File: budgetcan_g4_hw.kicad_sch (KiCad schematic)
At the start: 95 parts, among them IC1 M74VHC1GT66DTT1G, IC2 M74VHC1GT66DTT1G, IC3 M74VHC1GT66DTT1G, J1 USB_C_Receptacle_USB2.0, J3 20021511-00014T4LF, J4 Conn_01x02, J5 348260124, U1 AP22804AW5, U12 TJA1021T, U14 TPS2116DRLR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

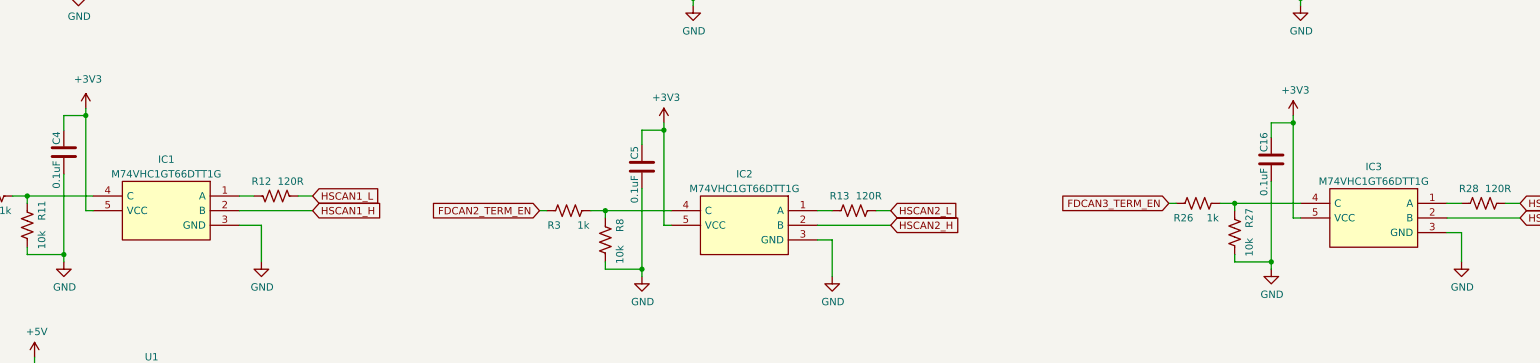
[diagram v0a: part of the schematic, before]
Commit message: Fix the LCSC part number for the CAN termination switch
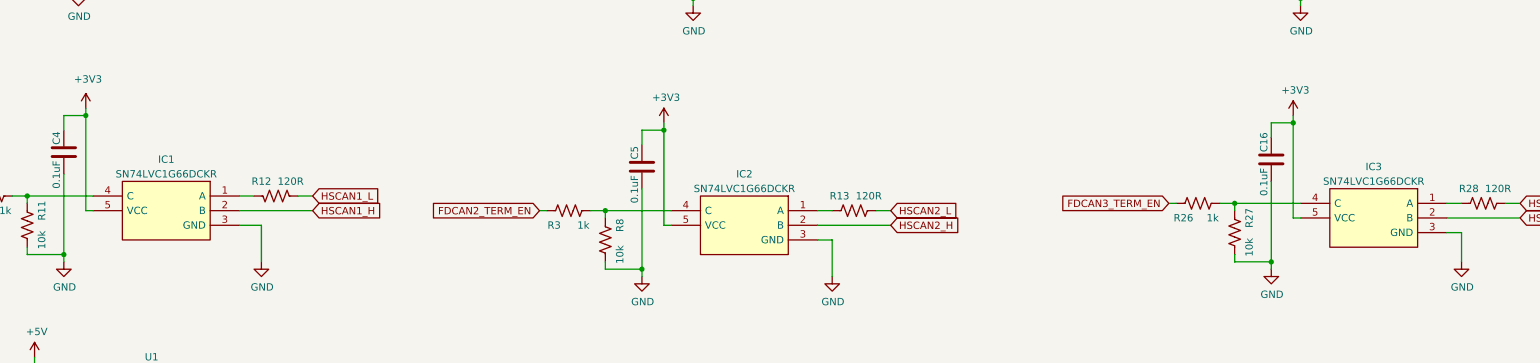
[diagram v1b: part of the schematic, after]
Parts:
- IC1, IC2, IC3: value M74VHC1GT66DTT1G -> SN74LVC1G66DCKR; LCSC Part # C5375974 -> C113518; Mouser Part Number 595-LVC1G66QDCKRQ1 -> (none); Mouser Price/Stock https://www.mouser.co.uk/ProductDetail/Texas-Instruments/SN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 -> (none)
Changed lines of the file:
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@@
       (effects (font (size 1.27 1.27)))
     )
-    (property "Value" "M74VHC1GT66DTT1G" (at 307.34 137.16 0)
+    (property "Value" "SN74LVC1G66DCKR" (at 307.34 137.16 0)
       (effects (font (size 1.27 1.27)))
     )
@@
       (effects (font (size 1.27 1.27)) (justify left) hide)
     )
-    (property "Mouser Part Number" "595-LVC1G66QDCKRQ1" (at 341.63 148.59 0)
-      (effects (font (size 1.27 1.27)) (justify left) hide)
-    )
-    (property "Mouser Price/Stock" "https://www.mouser.co.uk/ProductDetail/Texas-Instruments/SN74LVC1G66QDCKRQ1?qs=pajgIaoyDUhMU131%252BNzplA%3D%3D" (at 341.63 151.13 0)
+    (property "Mouser Part Number" "" (at 341.63 148.59 0)
+      (effects (font (size 1.27 1.27)) (justify left) hide)
+    )
+    (property "Mouser Price/Stock" "" (at 341.63 151.13 0)
       (effects (font (size 1.27 1.27)) (justify left) hide)
     )
@@
       (effects (font (size 1.27 1.27)) (justify left) hide)
     )
-    (property "LCSC Part #" "C5375974" (at 320.04 140.97 0)
+    (property "LCSC Part #" "C113518" (at 320.04 140.97 0)
       (effects (font (size 1.27 1.27)) hide)
     )
@@
       (effects (font (size 1.27 1.27)))
     )
-    (property "Value" "M74VHC1GT66DTT1G" (at 407.67 139.7 0)
+    (property "Value" "SN74LVC1G66DCKR" (at 407.67 139.7 0)
       (effects (font (size 1.27 1.27)))
     )
@@
       (effects (font (size 1.27 1.27)) (justify left) hide)
     )
-    (property "Mouser Part Number" "595-LVC1G66QDCKRQ1" (at 441.96 151.13 0)
-      (effects (font (size 1.27 1.27)) (justify left) hide)
-    )
-    (property "Mouser Price/Stock" "https://www.mouser.co.uk/ProductDetail/Texas-Instruments/SN74LVC1G66QDCKRQ1?qs=pajgIaoyDUhMU131%252BNzplA%3D%3D" (at 441.96 153.67 0)
+    (property "Mouser Part Number" "" (at 441.96 151.13 0)
+      (effects (font (size 1.27 1.27)) (justify left) hide)
+    )
+    (property "Mouser Price/Stock" "" (at 441.96 153.67 0)
       (effects (font (size 1.27 1.27)) (justify left) hide)
     )
@@
       (effects (font (size 1.27 1.27)) (justify left) hide)
     )
-    (property "LCSC Part #" "C5375974" (at 420.37 143.51 0)
+    (property "LCSC Part #" "C113518" (at 420.37 143.51 0)
       (effects (font (size 1.27 1.27)) hide)
     )
@@
       (effects (font (size 1.27 1.27)))
     )
-    (property "Value" "M74VHC1GT66DTT1G" (at 516.89 138.43 0)
+    (property "Value" "SN74LVC1G66DCKR" (at 516.89 138.43 0)
       (effects (font (size 1.27 1.27)))
     )
@@
       (effects (font (size 1.27 1.27)) (justify left) hide)
     )
-    (property "Mouser Part Number" "595-LVC1G66QDCKRQ1" (at 551.18 149.86 0)
-      (effects (font (size 1.27 1.27)) (justify left) hide)
-    )
-    (property "Mouser Price/Stock" "https://www.mouser.co.uk/ProductDetail/Texas-Instruments/SN74LVC1G66QDCKRQ1?qs=pajgIaoyDUhMU131%252BNzplA%3D%3D" (at 551.18 152.4 0)
+    (property "Mouser Part Number" "" (at 551.18 149.86 0)
+      (effects (font (size 1.27 1.27)) (justify left) hide)
+    )
+    (property "Mouser Price/Stock" "" (at 551.18 152.4 0)
       (effects (font (size 1.27 1.27)) (justify left) hide)
     )
@@
       (effects (font (size 1.27 1.27)) (justify left) hide)
     )
-    (property "LCSC Part #" "C5375974" (at 529.59 142.24 0)
-      (effects (font (size 1.27 1.27)) hide)
-    )
+    (property "LCSC Part #" "C113518" (at 529.59 142.24 0)
+      (effects (font (size 1.27 1.27)) hide)
+    )

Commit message: Fix incorrect connection of the 3.3V regulator feedback resistors
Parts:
- removed IC3: SN74LVC1G66DCKR, Package_TO_SOT_SMD:SOT-353_SC-70-5, symbol SamacSys_Parts:SN74LVC1G66QDCKRQ1
- added IC4: SN74LVC1G66DBVR, Package_TO_SOT_SMD:SOT-23-5, symbol SamacSys_Parts:SN74LVC1G66QDCKRQ1
- IC1, IC2: value SN74LVC1G66DCKR -> SN74LVC1G66DBVR; footprint Package_TO_SOT_SMD:SOT-353_SC-70-5 -> Package_TO_SOT_SMD:SOT-23-5; Height 1.1 -> (none); LCSC Part # C113518 -> C5375974; Manufacturer_Name Texas Instruments -> (none); Manufacturer_Part_Number SN74LVC1G66QDCKRQ1 -> SN74LVC1G66DBVR
- R18: value 20k -> 100k; LCSC Part # C25765 -> C25741
- R19: value 100k -> 20k; LCSC Part # C25741 -> C25765
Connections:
- net +3V3: now also IC4.5 (VCC); no longer R19.1
- net GND: now also IC4.3 (GND)
- net HSCAN2_H: now also IC4.2 (B); no longer IC2.2 (B)
- net HSCAN3_H: now also IC2.2 (B)
- net at R3.2, R8.1: now also IC4.4 (C); no longer IC2.4 (C)
- net at R28.1: now also IC2.1 (A)
- net at R18.2, U9.2 (FB): now also R19.1
- net at R13.1: now also IC4.1 (A); no longer IC2.1 (A)
- net at R26.2, R27.1: now also IC2.4 (C)
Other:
- moved on the sheet: C23, C26, R18, R19, U9

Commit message: Update to KiCad 8 and fix USB pinouts
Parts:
- removed R15, R20: 0R, Resistor_SMD:R_0603_1608Metric, symbol Device:R_US
- R1: now fitted
- R18: footprint Resistor_SMD:R_0402_1005Metric -> Resistor_SMD:R_0603_1608Metric; LCSC Part # C25741 -> C25803
- R19: footprint Resistor_SMD:R_0402_1005Metric -> Resistor_SMD:R_0603_1608Metric; LCSC Part # C25765 -> C4184
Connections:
- net USB_N: now also U3.6 (I/O1), U6.33 (PA11); no longer U6.32 (PA10)
- net USB_P: now also U3.4 (I/O2), U6.34 (PA12); no longer U6.33 (PA11)
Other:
- title: Budgetcan STM32G0B1xx -> budgetcan_g4

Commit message: Changes to fix issues found with prototype
- Fixed the power feed for FDCAN1 from switching the 5V feed (VCC) to the 3.3V feed (VIO)
- Changed the XTAL to 8Mhz
- Added a SW controlled master switch for LIN
- Changed the boot selector to a button switch
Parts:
- removed D8: LED_RED, LED_SMD:LED_0603_1608Metric, symbol Device:LED
- removed D9: ‎1N4448WX-TP‎, Diode_SMD:D_SOD-323, symbol Device:D
- removed J4: Conn_01x02, Connector_PinHeader_2.54mm:PinHeader_1x02_P2.54mm_Vertical, symbol Connector_Generic:Conn_01x02
- removed R17: 1k, Resistor_SMD:R_0402_1005Metric, symbol Device:R_US
- removed R29: 2.2k, Resistor_SMD:R_0603_1608Metric, symbol Device:R_US
- added D2: ‎1N4448WX-TP‎, Diode_SMD:D_SOD-323, symbol Device:D
- added Q1: 2N7002, Package_TO_SOT_SMD:SOT-23, symbol Transistor_FET:2N7002
- added Q2: MMBT3904, Package_TO_SOT_SMD:SOT-23, symbol Transistor_BJT:MMBT3904
- added R15: 0R, Resistor_SMD:R_0402_1005Metric, symbol Device:R_US
- added R20, R22: 1k, Resistor_SMD:R_0402_1005Metric, symbol Device:R_US
- added R21: 10k, Resistor_SMD:R_0402_1005Metric, symbol Device:R_US
- added SW1: TS-1088-AR02016, jlcpcb_parts:SW-SMD_L3.9-W3.0-P4.45, symbol jlcpcb_parts:TS-1088-AR02016
- D3, D4: footprint LED_SMD:LED_0603_1608Metric -> LED_SMD:LED_0805_2012Metric; Digi-Key_PN 475-2512-1-ND -> (none); LCSC Part # C2286 -> C84256; Manufacturer_Part_Number LS Q976-NR-1 -> (none)
- D6: footprint LED_SMD:LED_0603_1608Metric -> LED_SMD:LED_0805_2012Metric; Digi-Key_PN 475-2815-1-ND -> (none); LCSC Part # C965807 -> C965817; Manufacturer_Part_Number LB Q39E-N1OO-35-1 -> (none)
- D7: footprint LED_SMD:LED_0603_1608Metric -> LED_SMD:LED_0805_2012Metric; Digi-Key_PN 475-3754-1-ND -> (none); LCSC Part # C965804 -> C2297; Manufacturer_Part_Number LG Q396-PS-35 -> (none)
- F3: footprint Fuse:Fuse_1812_4532Metric -> jlcpcb_parts:F1812
- J3: LCSC Part # (none) -> C2881789
- J5: footprint kicad_lceda:CONN-TH_348260124 -> jlcpcb_parts:CONN-TH_348260124
- U14: footprint Package_TO_SOT_SMD:SOT-583-8 -> jlcpcb_parts:SOT-583-8_L2.1-W1.6-P0.50-LS1.6-BL
- U9: footprint Package_SON:WSON-6-1EP_2x2mm_P0.65mm_EP1x1.6mm_ThermalVias -> jlcpcb_parts:WSON-6_L2.0-W2.0-P0.65-TL-EP
- Y1: value 12Mhz -> 8Mhz; LCSC Part # C9002 -> C963531
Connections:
- net +12V: now also Q1.3 (D), R21.1
- net +3V3: now also C8.1, U1.5 (IN), R15.1, SW1.2; no longer C21.1, U4.5 (VIO), U4.8 (S)
- net +5V: now also C24.2, U4.3 (VCC); no longer C8.1, U1.5 (IN)
- net FDCAN1_RX_BOOT0: now also SW1.1
- net FDCAN1_SLEEP_EN: now also U4.8 (S); no longer R10.1, U1.4 (EN)
- net GND: now also Q2.2 (E)
- net LIN1_MASTER_SW: now reaches U6.15 (PA7)
- net LIN1_MASTER_SW: now also R20.1
- net FDCAN1_VIO_EN: now reaches U6.32 (PA10)
- net FDCAN1_VIO_EN: now also R10.1, U1.4 (EN)
- removed net FDCAN1_VCC: C24.2, U1.1 (OUT), U4.3 (VCC)
- net LIN1_NSLP renamed LIN1_NSLEEP
- net LIN_1 renamed LIN1
- net LIN1: now also R22.1
- new net: Q2.1 (B), R20.2
- new net: D2.1 (K), R22.2
- new net: D2.2 (A), Q1.2 (S)
- new net: Q1.1 (G), Q2.3 (C), R21.2
- new net FDCAN1_VIO: C21.1, R15.2, U1.1 (OUT), U4.5 (VIO)
- no-connect marks 25 -> 23
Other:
- moved on the sheet: C1, C2, C21, C24, C5, CR1, D10, IC4, R1, R13, R16, R2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
